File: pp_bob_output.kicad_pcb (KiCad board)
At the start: 2 copper layers, 98.8 x 72.1 mm, 31 parts, among them P4 13X2, U1 74LS540, U2 74LVC245, U3 74LS541

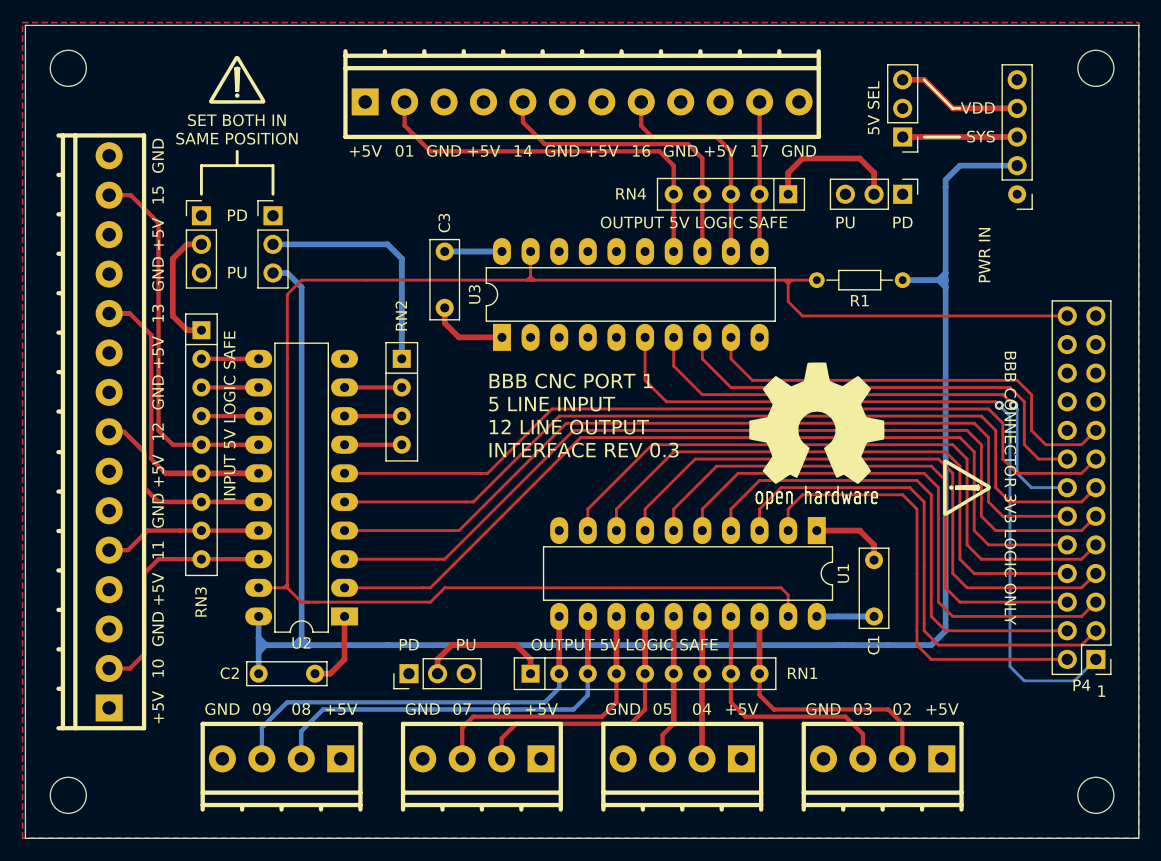
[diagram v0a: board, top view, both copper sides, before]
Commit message: Rotated Pu-Pd headers for U2 & U3 cleaned up silkscreen
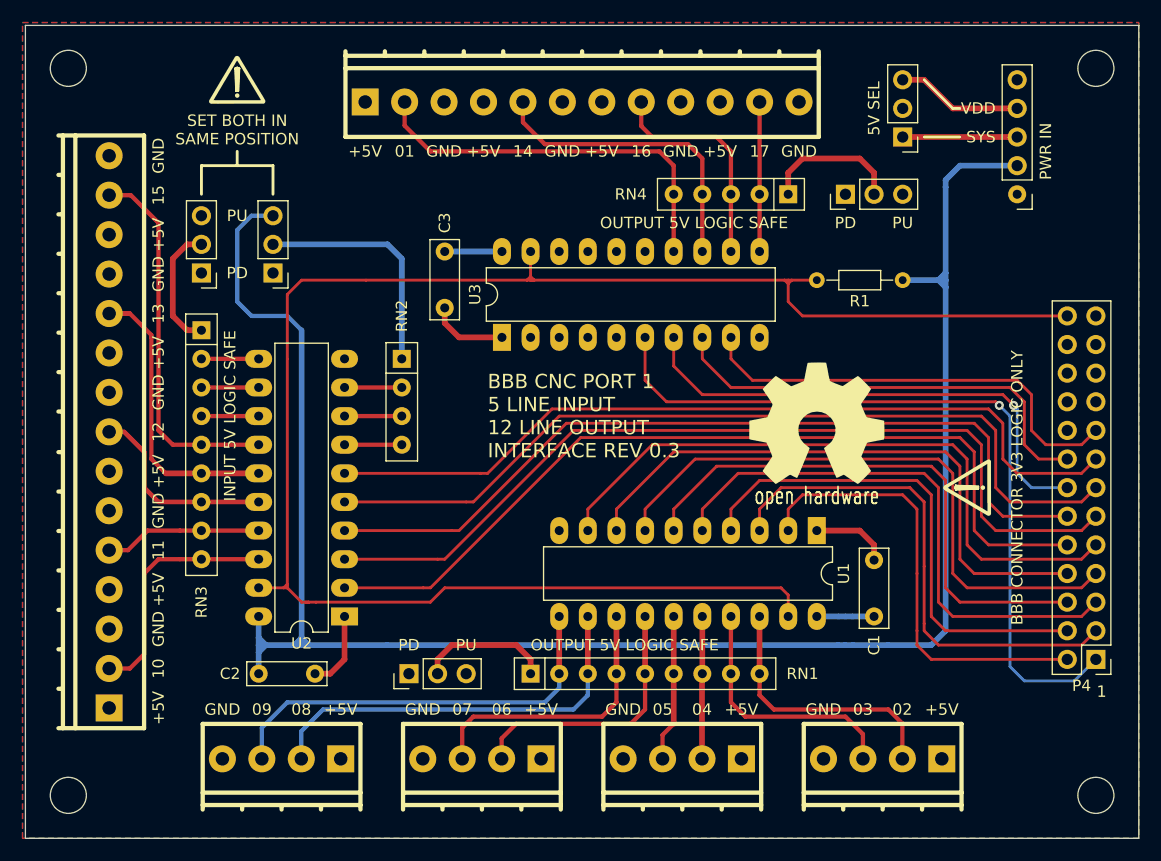
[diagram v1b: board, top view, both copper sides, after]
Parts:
- moved SEL_2 5.08 mm to (47.4, 47.4), turned to 180 degrees
- moved SEL_3 5.08 mm to (41.0, 47.4), turned to 180 degrees
- moved SEL_4 5.08 mm to (98.2, 40.4), turned to 90 degrees
- turned G*** to 90 degrees
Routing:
- net +3V3: track 157.5 -> 167.4 mm

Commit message: Modified schematic for seperate termianls, PCB modded with terminals spaced equally. Tracks to be rerouted
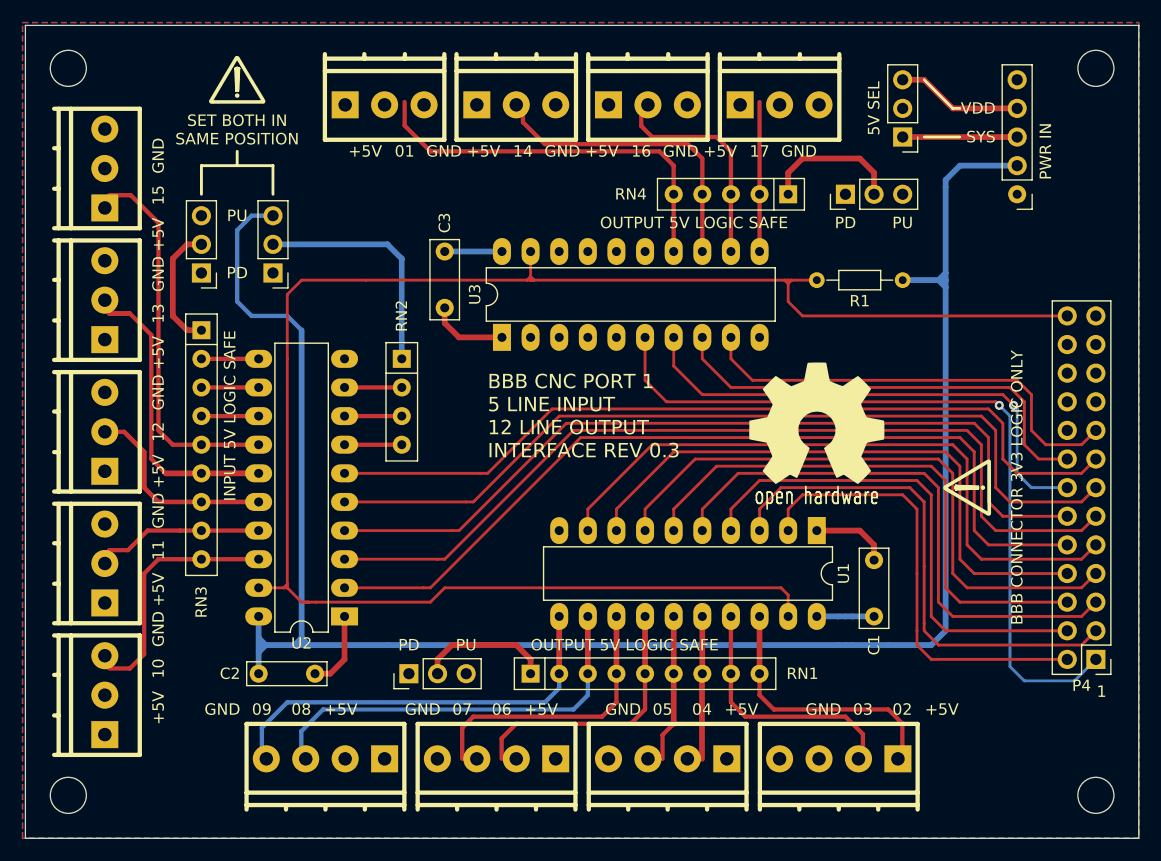
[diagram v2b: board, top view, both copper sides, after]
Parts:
- added J_OUT_1: ST_1x04, w_conn_pt-1,5:pt_1,5-4-3,5-h, F.Cu at (52.0, 91.2)
- added J_OUT_3: ST_1x04, w_conn_pt-1,5:pt_1,5-4-3,5-h, F.Cu at (82.4, 91.2)
- added J_OUT_4: ST_1x04, w_conn_pt-1,5:pt_1,5-4-3,5-h, F.Cu at (97.6, 91.2)
- added J_OUT_5: ST_1x03, w_conn_pt-1,5:pt_1,5-3-3,5-h, F.Cu at (57.3, 31.8)
- added J_OUT_6: ST_1x03, w_conn_pt-1,5:pt_1,5-3-3,5-h, F.Cu at (69.0, 31.8)
- added J_OUT_7: ST_1x03, w_conn_pt-1,5:pt_1,5-3-3,5-h, F.Cu at (80.6, 31.8)
- added J_OUT_8: ST_1x03, w_conn_pt-1,5:pt_1,5-3-3,5-h, F.Cu at (92.3, 31.8)
- J_IN_1, J_IN_2, J_IN_3, J_IN_4: value ST_1x04 -> ST_1x03; footprint w_conn_pt-1,5:pt_1,5-4-3,5-h -> w_conn_pt-1,5:pt_1,5-3-3,5-h
- J_IN_5: value ST_1x15 -> ST_1x03; footprint w_conn_pt-1,5:pt_1,5-15-3,5-h -> w_conn_pt-1,5:pt_1,5-3-3,5-h
- J_OUT_2: value ST_1x12 -> ST_1x04; footprint w_conn_pt-1,5:pt_1,5-12-3,5-h -> w_conn_pt-1,5:pt_1,5-4-3,5-h
- moved J_IN_1 70.0 mm to (31.8, 84.8), turned to 270 degrees
- moved J_OUT_2 60.2 mm to (67.2, 91.2), turned to 0 degrees
- moved J_IN_2 55.0 mm to (31.8, 73.2), turned to 270 degrees
- moved J_IN_3 45.3 mm to (31.8, 61.5), turned to 270 degrees
- moved J_IN_4 44.5 mm to (31.8, 49.8), turned to 270 degrees
- moved J_IN_5 23.4 mm to (31.8, 38.1)
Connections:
- J_IN_1 pad 2: /IN-02 -> /IN-10
- J_IN_1 pad 3: /IN-03 -> GND
- J_IN_2 pad 2: /IN-04 -> /IN-11
- J_IN_2 pad 3: /IN-05 -> GND
- J_IN_3 pad 2: /IN-06 -> /IN-12
- J_IN_3 pad 3: /IN-07 -> GND
- J_IN_4 pad 2: /IN-08 -> /IN-13
- J_IN_4 pad 3: /IN-09 -> GND
- J_IN_5 pad 2: /IN-10 -> /IN-15
- J_OUT_2 pad 2: /OUT-01 -> /IN-04
- J_OUT_2 pad 3: GND -> /IN-05
- J_OUT_2 pad 4: +5V -> GND
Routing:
- net +5V: track 10.2 -> 38.9 mm
- net /IN-15: track 33.2 -> 9.42 mm
- net GND: track 20.9 -> 35.4 mm
- net /IN-10: track 21.5 -> 6.98 mm
- net /IN-02: track 24.5 -> 19.6 mm
- net /IN-08: track 36.2 -> 38.4 mm
- net /IN-03: track 22.7 -> 20.5 mm

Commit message: Fixed silkscreen & and other details, good for manu
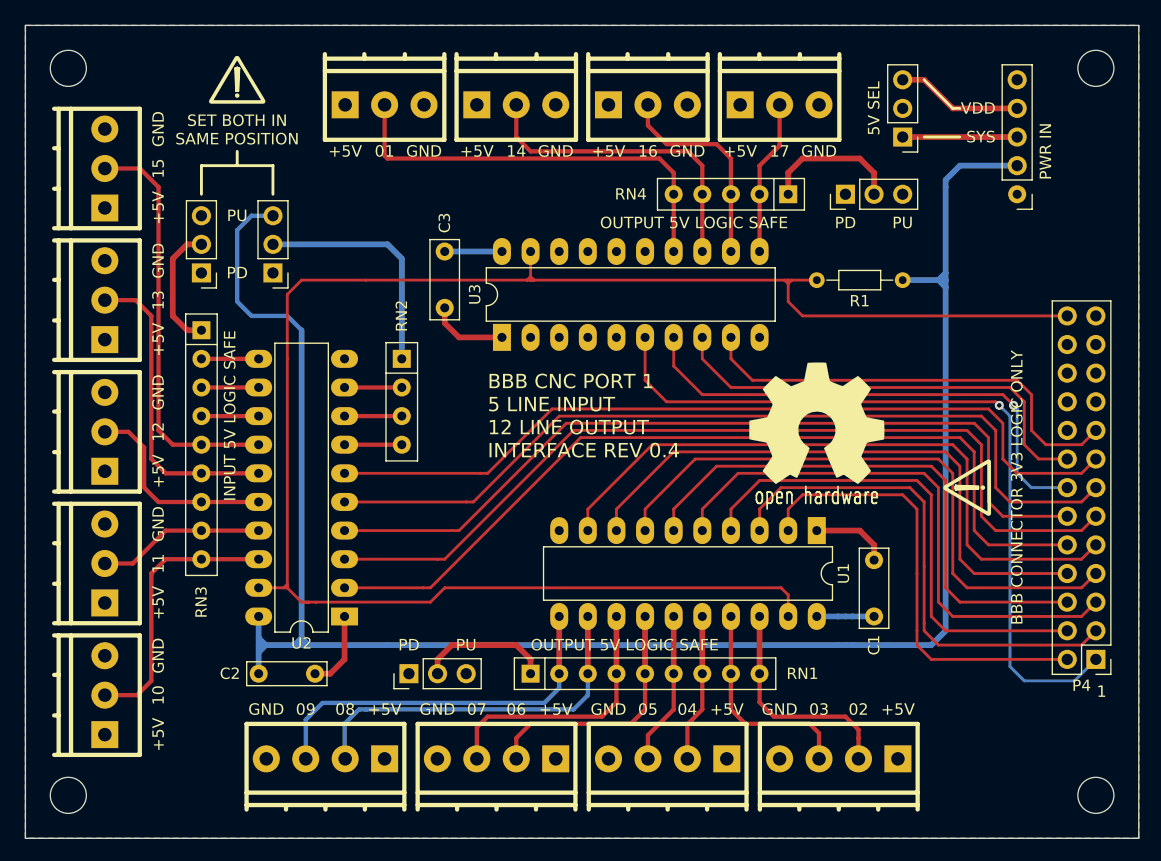
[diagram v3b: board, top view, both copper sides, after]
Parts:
- renumbered J_OUT_4 to J_OUT_1, J_OUT_3 to J_OUT_2, J_OUT_2 to J_OUT_3, J_OUT_1 to J_OUT_4
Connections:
- J_OUT_1 pad 2: /IN-08 -> /OUT-02
- J_OUT_1 pad 3: /IN-09 -> /OUT-03
- J_OUT_2 pad 2: /IN-06 -> /OUT-04
- J_OUT_2 pad 3: /IN-07 -> /OUT-05
- J_OUT_3 pad 2: /IN-04 -> /OUT-06
- J_OUT_3 pad 3: /IN-05 -> /OUT-07
- J_OUT_4 pad 2: /IN-02 -> /OUT-08
- J_OUT_4 pad 3: /IN-03 -> /OUT-09
- RN1 pad 2: /IN-09 -> /OUT-09
- RN1 pad 3: /IN-08 -> /OUT-08
- RN1 pad 4: /IN-07 -> /OUT-07
- RN1 pad 5: /IN-06 -> /OUT-06
- RN1 pad 6: /IN-05 -> /OUT-05
- RN1 pad 7: /IN-04 -> /OUT-04
- RN1 pad 8: /IN-03 -> /OUT-03
- RN1 pad 9: /IN-02 -> /OUT-02
- U1 pad 11: /IN-09 -> /OUT-09
- U1 pad 12: /IN-08 -> /OUT-08
- U1 pad 13: /IN-07 -> /OUT-07
- U1 pad 14: /IN-06 -> /OUT-06
- U1 pad 15: /IN-05 -> /OUT-05
- U1 pad 16: /IN-04 -> /OUT-04
- U1 pad 17: /IN-03 -> /OUT-03
- U1 pad 18: /IN-02 -> /OUT-02
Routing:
- net /IN-08: track 38.4 -> 0.00 mm
- net /IN-09: track 37.0 -> 0.00 mm
- net /OUT-09: track 0.00 -> 33.5 mm
- net /OUT-08: track 0.00 -> 32.8 mm
- net +5V: track 38.9 -> 10.2 mm
- net /IN-15: track 9.42 -> 36.5 mm
- net /IN-07: track 25.0 -> 0.00 mm
- net /IN-06: track 23.9 -> 0.00 mm
- net /OUT-07: track 0.00 -> 23.7 mm
- net /OUT-06: track 0.00 -> 22.6 mm
- net /OUT-02: track 0.00 -> 20.6 mm
- net /IN-03: track 20.5 -> 0.00 mm
- net /IN-02: track 19.6 -> 0.00 mm
- net /OUT-03: track 0.00 -> 19.2 mm
- net /IN-10: track 6.98 -> 24.2 mm
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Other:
- board text added: "BBB CNC PORT 1 5 LINE INPUT 12 LINE OUTPUT INTERFACE REV 0.4"
- board text removed: "BBB CNC PORT 1 5 LINE INPUT 12 LINE OUTPUT INTERFACE REV 0.3"
